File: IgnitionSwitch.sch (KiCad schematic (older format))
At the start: 10 parts, among them J7 BPS_PWR, SW8 SW_Rotary2x6, SW9 KILL_SW, U5 EL3H7, U6 EL3H7

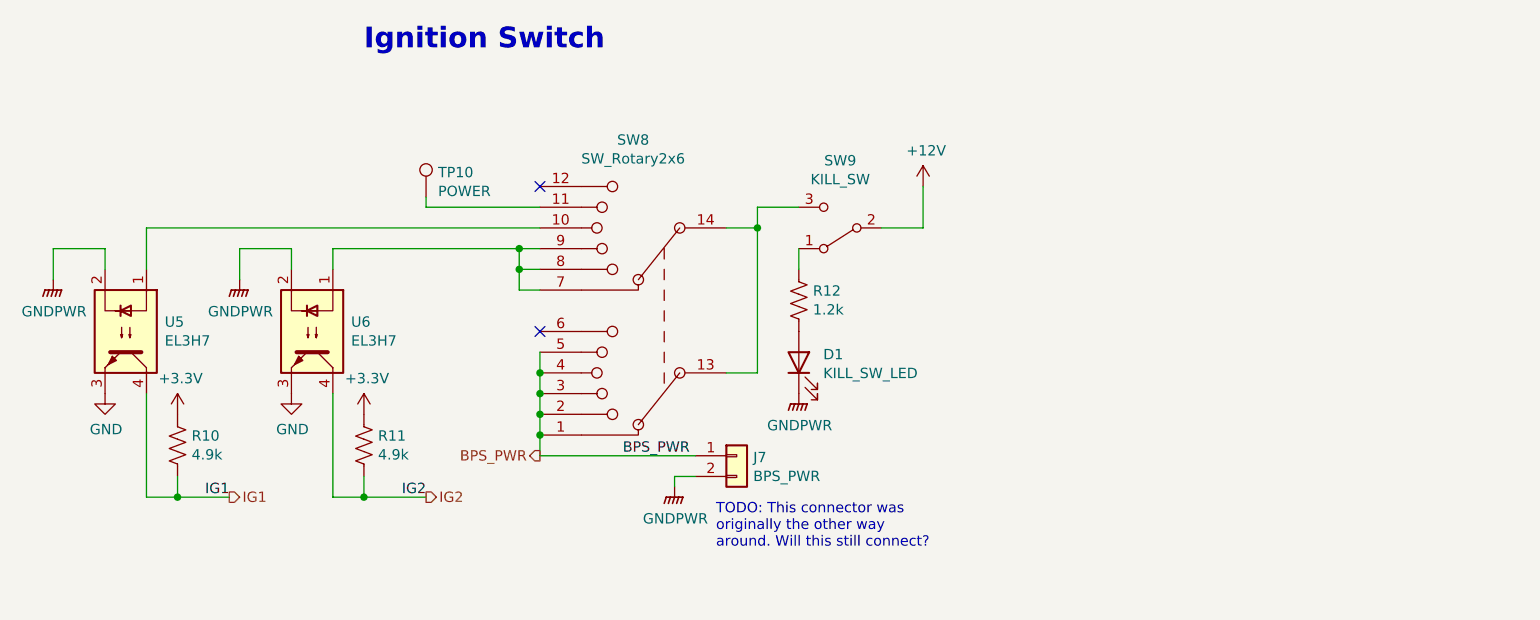
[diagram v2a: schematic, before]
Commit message: Finishes label and redesigns emergency switch/error light circuitry
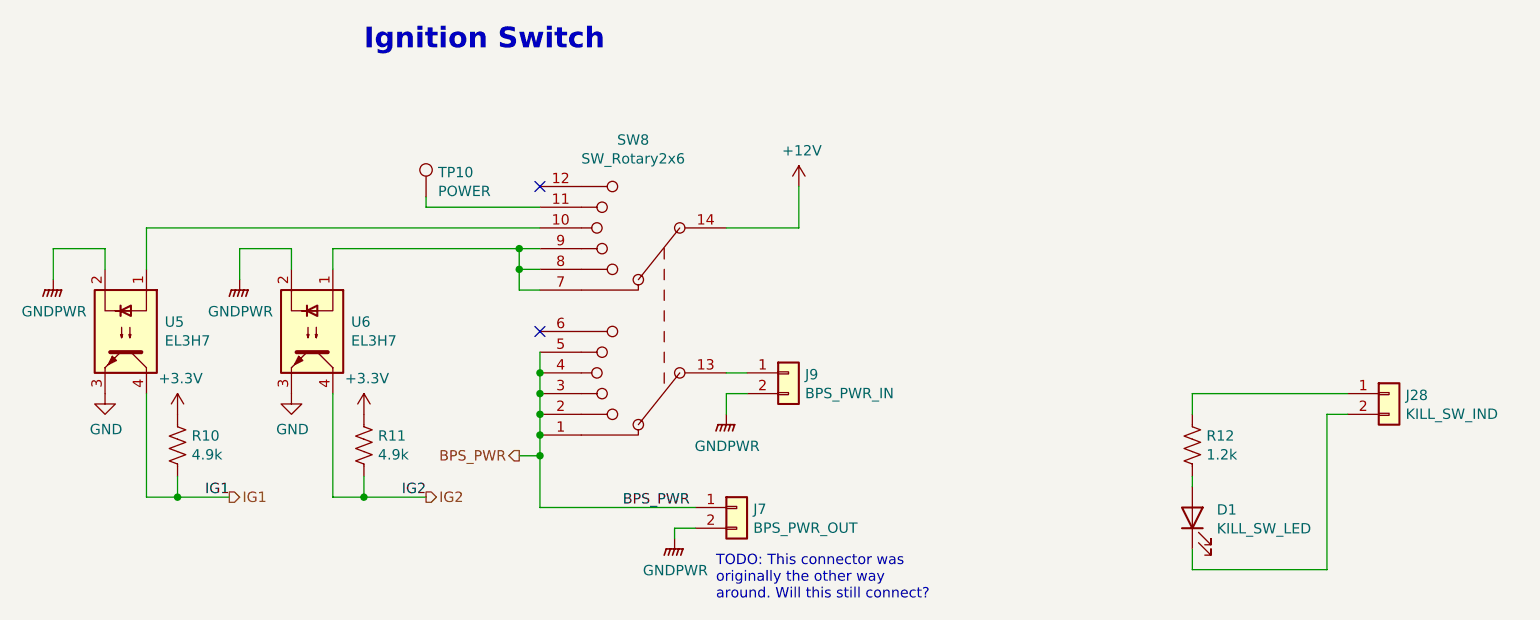
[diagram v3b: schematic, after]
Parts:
- removed SW9: KILL_SW, UTSVT_Connectors:Molex_MicroFit3.0_1x3xP3.00mm_PolarizingPeg_Vertical, symbol Switch:SW_SPDT
- added J28: KILL_SW_IND, UTSVT_Connectors:Molex_MicroFit3.0_1x2xP3.00mm_PolarizingPeg_Vertical, symbol Connector_Generic:Conn_01x02
- added J9: BPS_PWR_IN, UTSVT_Connectors:Molex_MicroFit3.0_1x2xP3.00mm_PolarizingPeg_Vertical, symbol Connector_Generic:Conn_01x02
- J7: value BPS_PWR -> BPS_PWR_OUT
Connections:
- net +12V: now also SW8.14
- net GNDPWR: now also J9.2 (Pin_2); no longer D1.1 (K)
- net at SW8.13: now also J9.1 (Pin_1); no longer SW8.14
- net at R12.1: now also J28.1 (Pin_1)
- new net: D1.1 (K), J28.2 (Pin_2)
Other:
- moved on the sheet: D1, J7, R12
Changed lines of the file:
@@
 	-1   0    0    1
 $EndComp
-$Comp
-L Switch:SW_SPDT SW?
-U 1 1 5F6BD6E3
-P 7400 3400
-AR Path="/5F6BD6E3" Ref="SW?"  Part="1"
-AR Path="/5F6B59CE/5F6BD6E3" Ref="SW9"  Part="1"
-F 0 "SW9" H 7400 3075 50  0000 C CNN
-F 1 "KILL_SW" H 7400 3166 50  0000 C CNN
-F 2 "UTSVT_Connectors:Molex_MicroFit3.0_1x3xP3.00mm_PolarizingPeg_Vertical" H 7400 3400 50  0001 C CNN
-F 3 "~" H 7400 3400 50  0001 C CNN
-	1    7400 3400
-	-1   0    0    1
-$EndComp
-$Comp
-L power:+12V #PWR?
-U 1 1 5F6BD6E9
-P 7800 3200
-AR Path="/5F6BD6E9" Ref="#PWR?"  Part="1"
-AR Path="/5F6B59CE/5F6BD6E9" Ref="#PWR0143"  Part="1"
-F 0 "#PWR0143" H 7800 3050 50  0001 C CNN
-F 1 "+12V" H 7815 3373 50  0000 C CNN
-F 2 "" H 7800 3200 50  0001 C CNN
-F 3 "" H 7800 3200 50  0001 C CNN
-	1    7800 3200
-	1    0    0    -1
-$EndComp
-Wire Wire Line
-	7800 3200 7800 3400
-Wire Wire Line
-	7800 3400 7600 3400
-Wire Wire Line
-	7200 3300 7000 3300
-Wire Wire Line
-	7000 3300 7000 3400
-Wire Wire Line
-	7000 3400 6850 3400
-Wire Wire Line
-	6850 4100 7000 4100
-Wire Wire Line
-	7000 4100 7000 3400
-Connection ~ 7000 3400
 Wire Wire Line
 	5950 4000 5950 4100
@@
 	5950 4300 5950 4400
 NoConn ~ 5950 3900
-$Comp
-L Device:R_US R?
-U 1 1 5F6BD700
-P 7200 3750
-AR Path="/5F6BD700" Ref="R?"  Part="1"
-AR Path="/5F6B59CE/5F6BD700" Ref="R12"  Part="1"
-F 0 "R12" H 7268 3796 50  0000 L CNN
-F 1 "1.2k" H 7268 3705 50  0000 L CNN
-F 2 "Resistor_SMD:R_0805_2012Metric" V 7240 3740 50  0001 C CNN
-F 3 "~" H 7200 3750 50  0001 C CNN
-F 4 "71-CRCW08051K20FKEA " H 7200 3750 50  0001 C CNN "Mouser Part Number"
-	1    7200 3750
-	1    0    0    -1
-$EndComp
-Wire Wire Line
-	7200 3500 7200 3600
-$Comp
-L Device:LED D?
-U 1 1 5F6BD707
-P 7200 4050
-AR Path="/5F6BD707" Ref="D?"  Part="1"
-AR Path="/5F6B59CE/5F6BD707" Ref="D1"  Part="1"
-F 0 "D1" V 7239 3932 50  0000 R CNN
-F 1 "KILL_SW_LED" V 7148 3932 50  0000 R CNN
-F 2 "UTSVT_Connectors:Molex_MicroFit3.0_1x2xP3.00mm_PolarizingPeg_Vertical" H 7200 4050 50  0001 C CNN
-F 3 "~" H 7200 4050 50  0001 C CNN
-	1    7200 4050
-	0    -1   -1   0
-$EndComp
-$Comp
-L power:GNDPWR #PWR?
-U 1 1 5F6BD70D
-P 7200 4200
-AR Path="/5F6BD70D" Ref="#PWR?"  Part="1"
-AR Path="/5F6B59CE/5F6BD70D" Ref="#PWR0144"  Part="1"
-F 0 "#PWR0144" H 7200 4000 50  0001 C CNN
-F 1 "GNDPWR" H 7204 4046 50  0000 C CNN
-F 2 "" H 7200 4150 50  0001 C CNN
-F 3 "" H 7200 4150 50  0001 C CNN
-	1    7200 4200
-	1    0    0    -1
-$EndComp
 Connection ~ 5950 4400
 NoConn ~ 5950 3200
@@
 Text Notes 5100 2550 0    100  ~ 20
 Ignition Switch
-$Comp
-L Connector_Generic:Conn_01x02 J?
-U 1 1 5F6BD77F
-P 6900 4500
-AR Path="/5F6BD77F" Ref="J?"  Part="1"
-AR Path="/5F6B59CE/5F6BD77F" Ref="J7"  Part="1"
-F 0 "J7" H 6980 4492 50  0000 L CNN
-F 1 "BPS_PWR" H 6980 4401 50  0000 L CNN
-F 2 "UTSVT_Connectors:Molex_MicroFit3.0_1x2xP3.00mm_PolarizingPeg_Vertical" H 6900 4500 50  0001 C CNN
-F 3 "~" H 6900 4500 50  0001 C CNN
-	1    6900 4500
-	1    0    0    -1
-$EndComp
-$Comp
-L power:GNDPWR #PWR?
-U 1 1 5F6BD785
-P 6600 4650
-AR Path="/5F6BD785" Ref="#PWR?"  Part="1"
-AR Path="/5F6B59CE/5F6BD785" Ref="#PWR0151"  Part="1"
-F 0 "#PWR0151" H 6600 4450 50  0001 C CNN
-F 1 "GNDPWR" H 6604 4496 50  0000 C CNN
-F 2 "" H 6600 4600 50  0001 C CNN
-F 3 "" H 6600 4600 50  0001 C CNN
-	1    6600 4650
-	1    0    0    -1
-$EndComp
-Wire Wire Line
-	6600 4650 6600 4600
-Wire Wire Line
-	6600 4600 6700 4600
 Wire Wire Line
 	5950 4400 5950 4500
-Wire Wire Line
-	6700 4500 5950 4500
-Text Label 6350 4500 0    50   ~ 0
-BPS_PWR
-Text Notes 6800 4950 0    50   ~ 0
-TODO: This connector was\noriginally the other way\naround. Will this still connect?
 Text HLabel 4450 4700 2    50   Output ~ 0
 IG1
 Text HLabel 5400 4700 2    50   Output ~ 0
 IG2
-Text HLabel 5950 4500 0    50   Output ~ 0
+$Comp
+L Connector_Generic:Conn_01x02 J?
+U 1 1 5F86B0FA
+P 10050 4200
+AR Path="/5F86B0FA" Ref="J?"  Part="1"
+AR Path="/5F6B59CE/5F86B0FA" Ref="J28"  Part="1"
+F 0 "J28" H 10130 4192 50  0000 L CNN
+F 1 "KILL_SW_IND" H 10130 4101 50  0000 L CNN
+F 2 "UTSVT_Connectors:Molex_MicroFit3.0_1x2xP3.00mm_PolarizingPeg_Vertical" H 10050 4200 50  0001 C CNN
+F 3 "~" H 10050 4200 50  0001 C CNN
+	1    10050 4200
+	1    0    0    -1
+$EndComp
+Wire Wire Line
+	9100 4200 9100 4300
+Wire Wire Line
+	9100 4650 9100 4600
+$Comp
+L Device:LED D?
+U 1 1 5F6BD707
+P 9100 4800
+AR Path="/5F6BD707" Ref="D?"  Part="1"
+AR Path="/5F6B59CE/5F6BD707" Ref="D1"  Part="1"
+F 0 "D1" V 9139 4682 50  0000 R CNN
+F 1 "KILL_SW_LED" V 9048 4682 50  0000 R CNN
+F 2 "UTSVT_Connectors:Molex_MicroFit3.0_1x2xP3.00mm_PolarizingPeg_Vertical" H 9100 4800 50  0001 C CNN
+F 3 "~" H 9100 4800 50  0001 C CNN
+	1    9100 4800
+	0    -1   -1   0
+$EndComp
+$Comp
+L Device:R_US R?
+U 1 1 5F6BD700
+P 9100 4450
+AR Path="/5F6BD700" Ref="R?"  Part="1"
+AR Path="/5F6B59CE/5F6BD700" Ref="R12"  Part="1"
+F 0 "R12" H 9168 4496 50  0000 L CNN
+F 1 "1.2k" H 9168 4405 50  0000 L CNN
+F 2 "Resistor_SMD:R_0805_2012Metric" V 9140 4440 50  0001 C CNN
+F 3 "~" H 9100 4450 50  0001 C CNN
+F 4 "71-CRCW08051K20FKEA " H 9100 4450 50  0001 C CNN "Mouser Part Number"
+	1    9100 4450
+	1    0    0    -1
+$EndComp
+Text Notes 6800 5200 0    50   ~ 0
+TODO: This connector was\noriginally the other way\naround. Will this still connect?
+Text Label 6350 4750 0    50   ~ 0
 BPS_PWR
+Wire Wire Line
+	6700 4750 5950 4750
+Wire Wire Line
+	6600 4850 6700 4850
+Wire Wire Line
+	6600 4900 6600 4850
+$Comp
+L power:GNDPWR #PWR?
+U 1 1 5F6BD785
+P 6600 4900
+AR Path="/5F6BD785" Ref="#PWR?"  Part="1"
+AR Path="/5F6B59CE/5F6BD785" Ref="#PWR0151"  Part="1"
+F 0 "#PWR0151" H 6600 4700 50  0001 C CNN
+F 1 "GNDPWR" H 6604 4746 50  0000 C CNN
+F 2 "" H 6600 4850 50  0001 C CNN
+F 3 "" H 6600 4850 50  0001 C CNN
+	1    6600 4900
+	1    0    0    -1
+$EndComp
+Text HLabel 5850 4500 0    50   Output ~ 0
+BPS_PWR
+$Comp
+L Connector_Generic:Conn_01x02 J?
+U 1 1 5F6BD77F
+P 6900 4750
+AR Path="/5F6BD77F" Ref="J?"  Part="1"
+AR Path="/5F6B59CE/5F6BD77F" Ref="J7"  Part="1"
+F 0 "J7" H 6980 4742 50  0000 L CNN
+F 1 "BPS_PWR_OUT" H 6980 4651 50  0000 L CNN
+F 2 "UTSVT_Connectors:Molex_MicroFit3.0_1x2xP3.00mm_PolarizingPeg_Vertical" H 6900 4750 50  0001 C CNN
+F 3 "~" H 6900 4750 50  0001 C CNN
+	1    6900 4750
+	1    0    0    -1
+$EndComp
+$Comp
+L power:+12V #PWR?
+U 1 1 5F6BD6E9
+P 7200 3200
+AR Path="/5F6BD6E9" Ref="#PWR?"  Part="1"
+AR Path="/5F6B59CE/5F6BD6E9" Ref="#PWR0143"  Part="1"
+F 0 "#PWR0143" H 7200 3050 50  0001 C CNN
+F 1 "+12V" H 7215 3373 50  0000 C CNN
+F 2 "" H 7200 3200 50  0001 C CNN
+F 3 "" H 7200 3200 50  0001 C CNN
+	1    7200 3200
+	1    0    0    -1
+$EndComp
+Wire Wire Line
+	7200 3200 7200 3400
+Wire Wire Line
+	6850 3400 7200 3400
+Wire Wire Line
+	5850 4500 5950 4500
+Wire Wire Line
+	5950 4500 5950 4750
+Connection ~ 5950 4500
+$Comp
+L Connector_Generic:Conn_01x02 J?
+U 1 1 5F8C3B18
+P 7150 4100
+AR Path="/5F8C3B18" Ref="J?"  Part="1"
+AR Path="/5F6B59CE/5F8C3B18" Ref="J9"  Part="1"
+F 0 "J9" H 7230 4092 50  0000 L CNN
+F 1 "BPS_PWR_IN" H 7230 4001 50  0000 L CNN
+F 2 "UTSVT_Connectors:Molex_MicroFit3.0_1x2xP3.00mm_PolarizingPeg_Vertical" H 7150 4100 50  0001 C CNN
+F 3 "~" H 7150 4100 50  0001 C CNN
+	1    7150 4100
+	1    0    0    -1
+$EndComp
+Wire Wire Line
+	6950 4100 6850 4100
+$Comp
+L power:GNDPWR #PWR?
+U 1 1 5F8C4E7D
+P 6850 4300
+AR Path="/5F8C4E7D" Ref="#PWR?"  Part="1"
+AR Path="/5F6B59CE/5F8C4E7D" Ref="#PWR0129"  Part="1"
+F 0 "#PWR0129" H 6850 4100 50  0001 C CNN
+F 1 "GNDPWR" H 6854 4146 50  0000 C CNN
+F 2 "" H 6850 4250 50  0001 C CNN
+F 3 "" H 6850 4250 50  0001 C CNN
+	1    6850 4300
+	1    0    0    -1
+$EndComp
+Wire Wire Line
+	6850 4300 6850 4200
+Wire Wire Line
+	6850 4200 6950 4200
+Wire Wire Line
+	9850 4200 9100 4200
+Wire Wire Line
+	9100 4950 9100 5050
+Wire Wire Line
+	9100 5050 9750 5050
+Wire Wire Line
+	9750 5050 9750 4300
+Wire Wire Line
+	9750 4300 9850 4300
 $EndSCHEMATC

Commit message: Adds connector for power secondary board
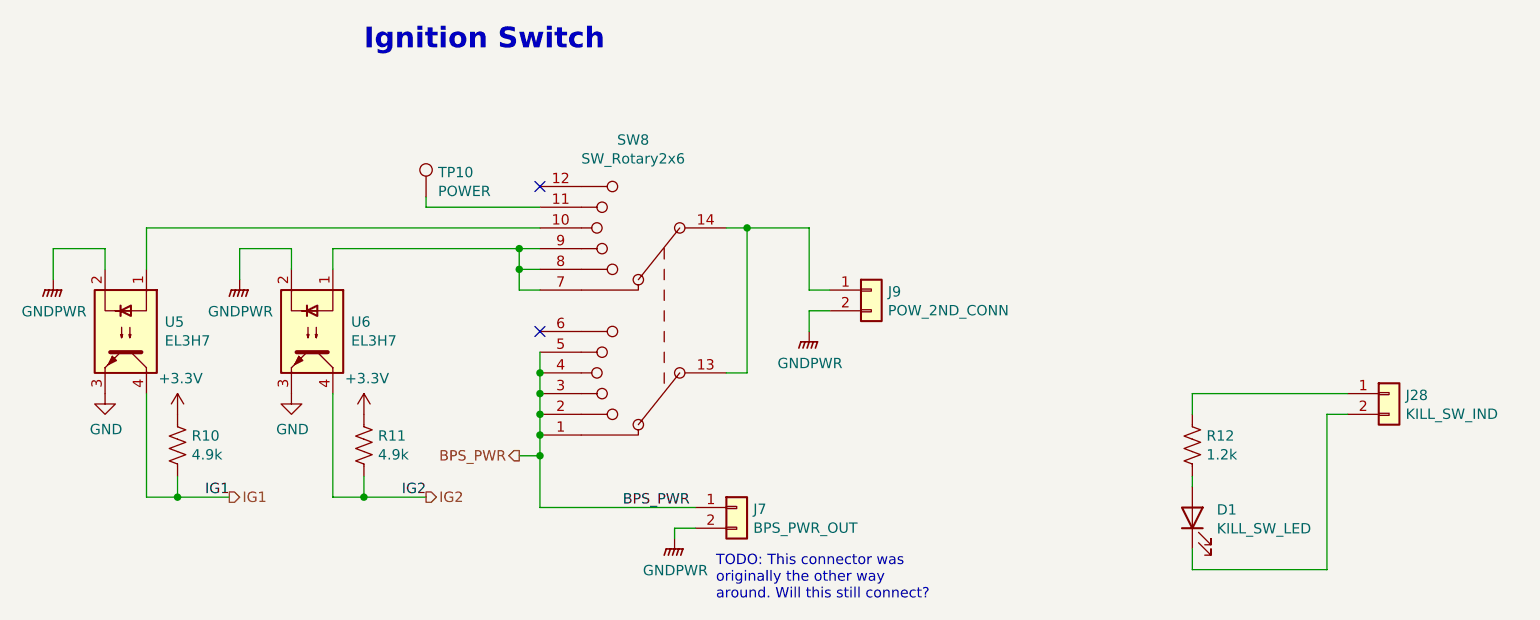
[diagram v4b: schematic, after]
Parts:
- J9: value BPS_PWR_IN -> POW_2ND_CONN
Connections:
- net +12V is gone; now on an unnamed net: SW8.14
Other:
- moved on the sheet: J9

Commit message: Connects pots to ADC pins and removes JTAG connections
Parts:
- SW8: footprint UTSVT_Special:CK1035 -> UTSVT_Special:CK1035_resized
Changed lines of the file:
@@
 $Descr A4 11693 8268
 encoding utf-8
-Sheet 7 10
+Sheet 6 10
 Title ""
 Date ""
@@
 F 0 "SW8" H 6500 2975 50  0000 C CNN
 F 1 "SW_Rotary2x6" H 6500 3066 50  0000 C CNN
-F 2 "UTSVT_Special:CK1035" H 6350 4400 50  0001 C CNN
+F 2 "UTSVT_Special:CK1035_resized" H 6350 4400 50  0001 C CNN
 F 3 "https://www.mouser.com/datasheet/2/242/CK-681.pdf" H 6350 4400 50  0001 C CNN
 F 4 "10WA325 " H 6450 3800 50  0001 C CNN "Mouser Part Number"

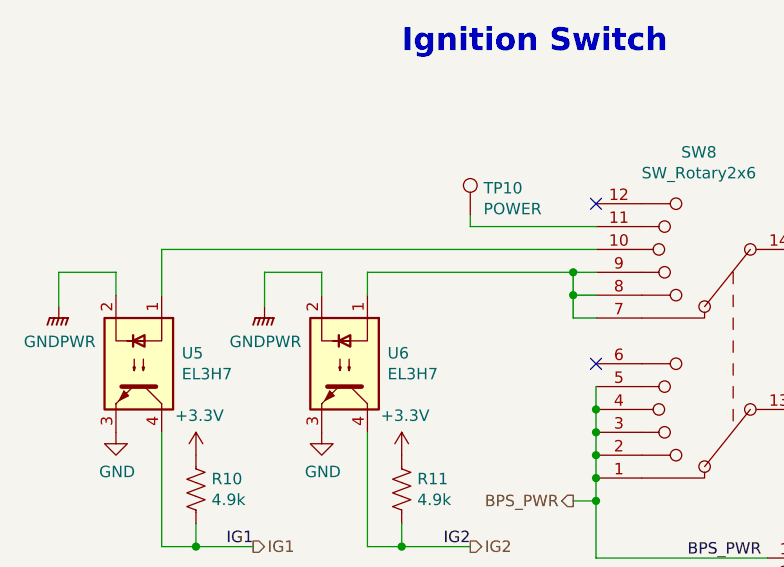
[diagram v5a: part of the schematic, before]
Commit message: Changes the layout of the board, adds resistors for ignition switch, and gives motar can isolated +12v, still need to change resistor value for the isolated +12v(didnt remember how to find the value)
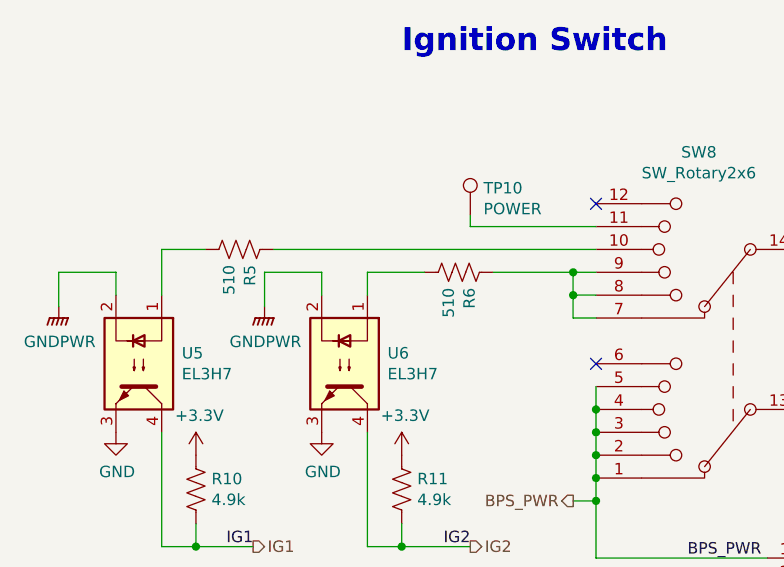
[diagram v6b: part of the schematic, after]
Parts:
- added R5, R6: 510, Resistor_SMD:R_0805_2012Metric, symbol Device:R_US
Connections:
- net at SW8.10: now also R5.1; no longer U5.1
- net at SW8.7, SW8.8, SW8.9: now also R6.1; no longer U6.1
- new net: R5.2, U5.1
- new net: R6.2, U6.1
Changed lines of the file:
@@
 $Descr A4 11693 8268
 encoding utf-8
-Sheet 6 10
+Sheet 5 10
 Title ""
 Date ""
@@
 Connection ~ 5850 3500
 Wire Wire Line
-	5850 3500 4950 3500
+	5850 3500 5500 3500
 Wire Wire Line
 	5950 3600 5850 3600
@@
 	4050 3400 4050 3600
 Wire Wire Line
-	4050 3400 5950 3400
+	4050 3400 4240 3400
 $Comp
 L power:GNDPWR #PWR?
@@
 Wire Wire Line
 	7250 3900 7250 3800
+$Comp
+L Device:R_US R?
+U 1 1 6190FB56
+P 5350 3500
+AR Path="/6190FB56" Ref="R?"  Part="1"
+AR Path="/5F6B59CE/6190FB56" Ref="R6"  Part="1"
+F 0 "R6" H 5418 3546 50  0000 L CNN
+F 1 "510" H 5418 3455 50  0000 L CNN
+F 2 "Resistor_SMD:R_0805_2012Metric" V 5390 3490 50  0001 C CNN
+F 3 "~" H 5350 3500 50  0001 C CNN
+F 4 "71-CRCW08054K99FKEAC " H 5350 3500 50  0001 C CNN "Mouser Part Number"
+	1    5350 3500
+	0    1    1    0
+$EndComp
+Wire Wire Line
+	5200 3500 4950 3500
+$Comp
+L Device:R_US R?
+U 1 1 61912237
+P 4390 3400
+AR Path="/61912237" Ref="R?"  Part="1"
+AR Path="/5F6B59CE/61912237" Ref="R5"  Part="1"
+F 0 "R5" H 4458 3446 50  0000 L CNN
+F 1 "510" H 4458 3355 50  0000 L CNN
+F 2 "Resistor_SMD:R_0805_2012Metric" V 4430 3390 50  0001 C CNN
+F 3 "~" H 4390 3400 50  0001 C CNN
+F 4 "71-CRCW08054K99FKEAC " H 4390 3400 50  0001 C CNN "Mouser Part Number"
+	1    4390 3400
+	0    1    1    0
+$EndComp
+Wire Wire Line
+	4540 3400 5950 3400
 $EndSCHEMATC
